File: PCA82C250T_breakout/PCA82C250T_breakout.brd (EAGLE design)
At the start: 100 x 80 mm, 0 parts

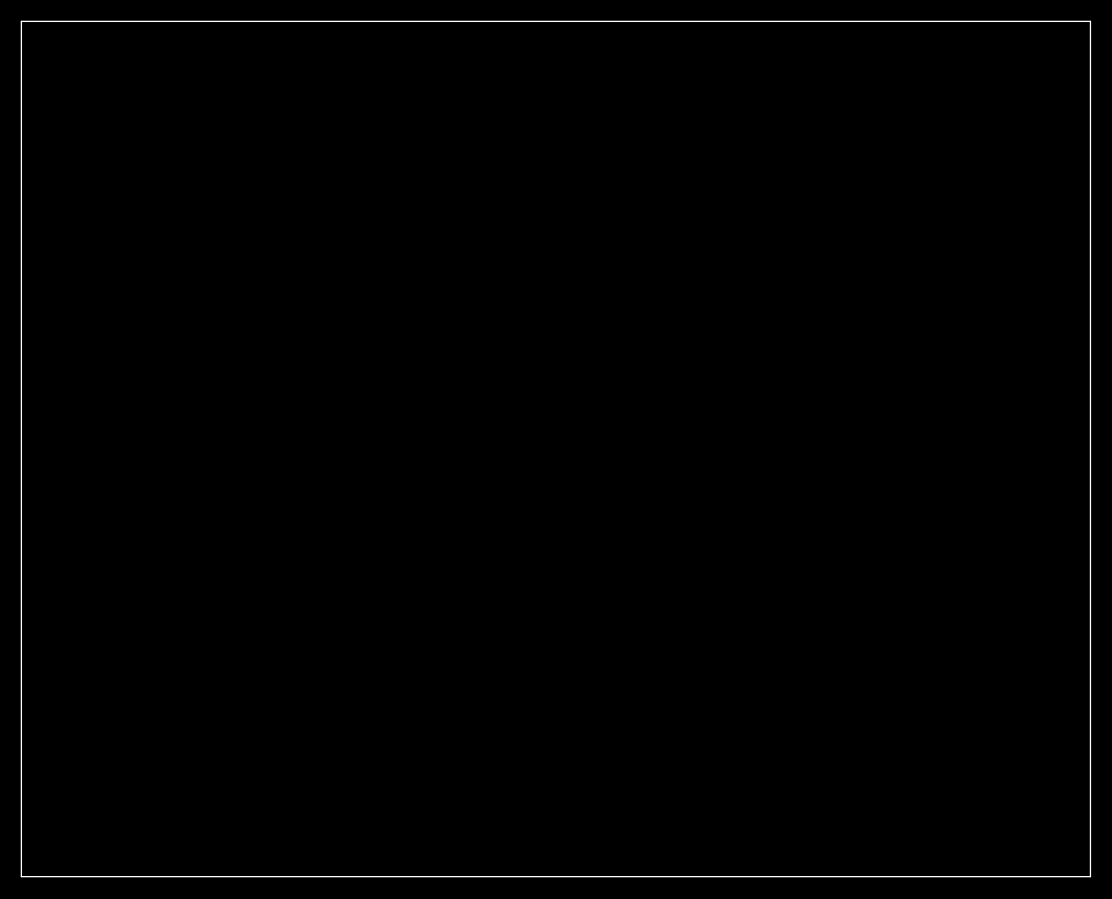
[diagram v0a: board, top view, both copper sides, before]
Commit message: * layed out can breakout PCB
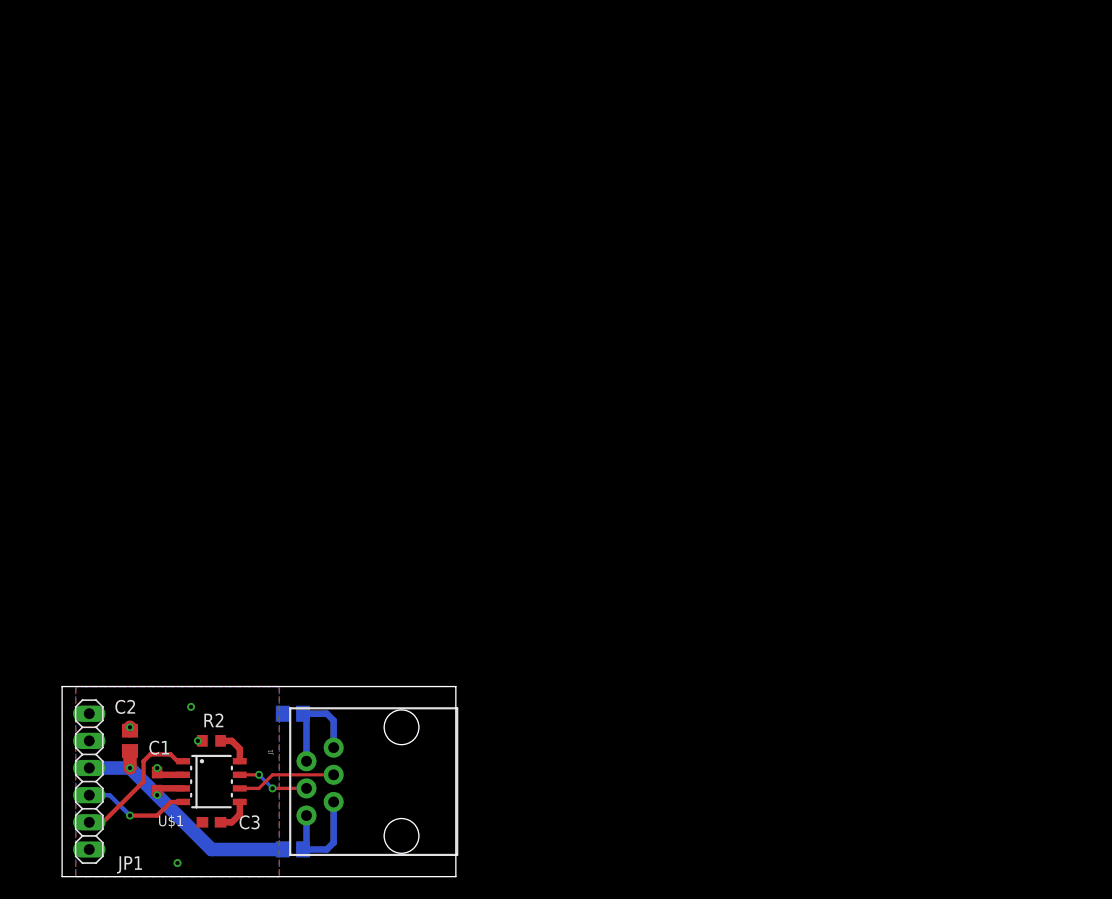
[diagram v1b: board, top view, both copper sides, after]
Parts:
- added C1: 100n, SquantorRCL:C0603
- added C2: 2.2u, SquantorRCL:C0805
- added C3: DNS, SquantorRCL:C0603
- added J1: RJ11, SparkFun-Connectors:RJ11-6
- added JP1: FTDI, SquantorConnectors:1X06
- added R1, R3: FB, SquantorRCL:R0805
- added R2: RS, SquantorRCL:R0603
- added U$1: PCA82C250, SquantorNxp:SOT96-1
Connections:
- new net +5V: C1.2, C2.2, JP1.3, R1.2, U$1.3
- new net CANH: J1.3, U$1.7
- new net CANL: J1.4, U$1.6
- new net GND: C1.1, C2.1, C3.1, JP1.1, R2.2, R3.1, U$1.2
- new net N$1: J1.1, J1.2, R1.1
- new net N$2: C3.2, U$1.5
- new net N$3: J1.5, J1.6, R3.2
- new net N$5: R2.1, U$1.8
- new net UART_RX: JP1.5, U$1.1
- new net UART_TX: JP1.4, U$1.4
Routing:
- net +5V: track 0.00 -> 25.9 mm, vias 0 -> 2
- net UART_RX: track 0.00 -> 12.8 mm
- net N$3: track 0.00 -> 10.1 mm
- net N$1: track 0.00 -> 10.1 mm
- net UART_TX: track 0.00 -> 10.1 mm, vias 0 -> 1
- net CANL: track 0.00 -> 9.31 mm
- net CANH: track 0.00 -> 6.77 mm, vias 0 -> 2
- net GND: track 0.00 -> 3.81 mm, vias 0 -> 5
- net N$2: track 0.00 -> 3.27 mm
- net N$5: track 0.00 -> 3.27 mm
- added copper zone on layer 1, net GND
- added copper zone on layer 16, net GND
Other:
- board size 100 x 80 mm -> 36.8 x 17.8 mm

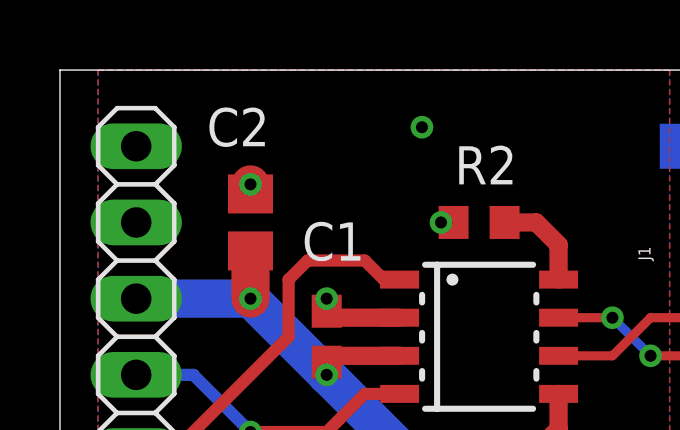
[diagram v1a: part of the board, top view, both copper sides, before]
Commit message: * small mods for OSHpark manufacturing
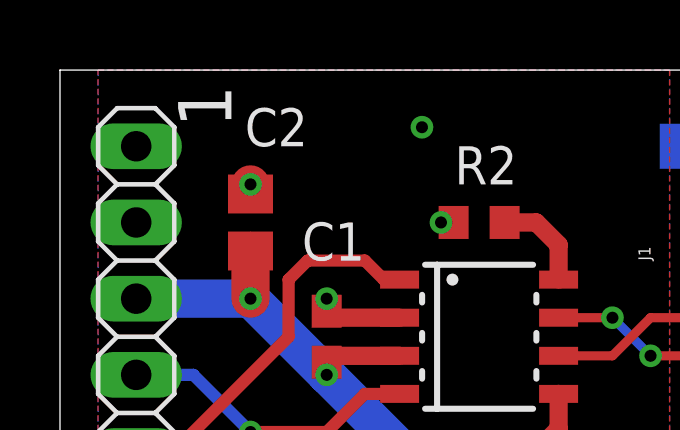
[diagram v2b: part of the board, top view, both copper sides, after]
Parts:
- added LOGO1: OSHW_LOGO_10MILX0200-NT, ohw-logo:OSHW_10X200_NOTEXT
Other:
- board text added: "1"
- board text added: "V2015.10.03"
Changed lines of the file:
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@@
 <wire x1="40.64" y1="17.78" x2="3.81" y2="17.78" width="0" layer="20"/>
 <wire x1="3.81" y1="17.78" x2="3.81" y2="0" width="0" layer="20"/>
+<text x="9.525" y="15.875" size="1.778" layer="25" font="vector" rot="R90">1</text>
+<text x="33.02" y="14.605" size="1.27" layer="26" font="vector" rot="MR270">V2015.10.03</text>
 </plain>
 <attributes>
@@
 <element name="C1" library="SquantorRCL" package="C0603" value="100n" x="12.7" y="8.89" smashed="yes" rot="R270">
 <attribute name="NAME" x="13.97" y="12.7" size="1.27" layer="25" rot="R180"/>
-<attribute name="VALUE" x="15.24" y="14.605" size="1.27" layer="27" rot="R180"/>
+<attribute name="VALUE" x="15.875" y="14.605" size="1.27" layer="27" rot="R180"/>
 </element>
 <element name="C2" library="SquantorRCL" package="C0805" value="2.2u" x="10.16" y="12.7" smashed="yes" rot="R270">
-<attribute name="NAME" x="10.795" y="16.51" size="1.27" layer="25" rot="R180"/>
-<attribute name="VALUE" x="15.24" y="16.51" size="1.27" layer="27" rot="R180"/>
+<attribute name="NAME" x="12.065" y="16.51" size="1.27" layer="25" rot="R180"/>
+<attribute name="VALUE" x="15.875" y="16.51" size="1.27" layer="27" rot="R180"/>
 </element>
 <element name="R1" library="SquantorRCL" package="R0805" value="FB" x="25.4" y="2.54" smashed="yes" rot="MR0">
@@
 <attribute name="VALUE" x="20.955" y="17.145" size="1.27" layer="28" rot="MR180"/>
 </element>
+<element name="LOGO1" library="ohw-logo" package="OSHW_10X200_NOTEXT" value="OSHW_LOGO_10MILX0200-NT" x="20.32" y="6.35" rot="MR0"/>
 </elements>
 <signals>

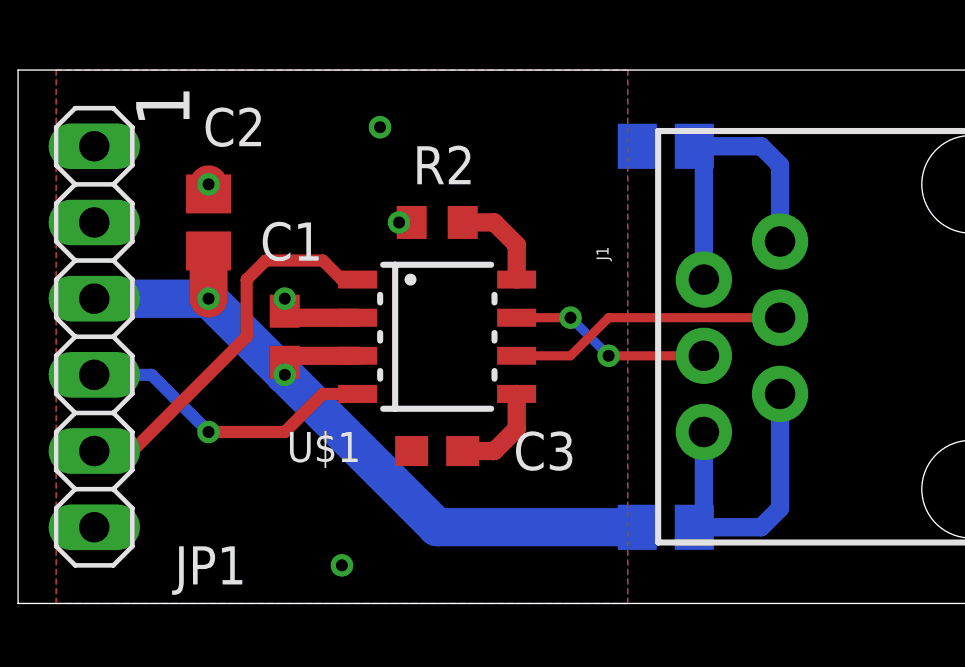
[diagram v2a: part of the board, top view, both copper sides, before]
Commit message: * added CAN termination resistor
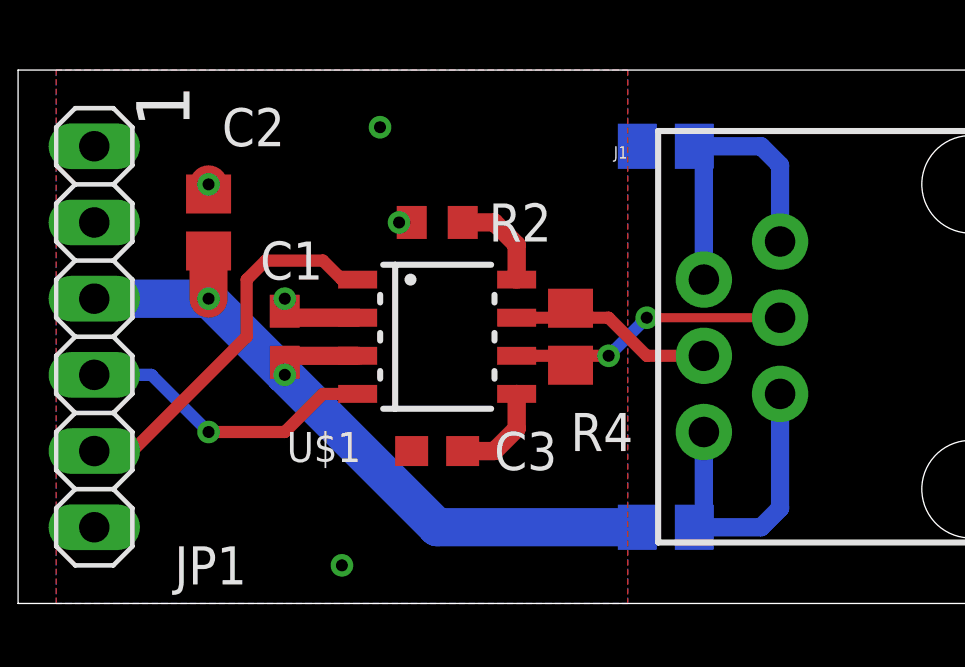
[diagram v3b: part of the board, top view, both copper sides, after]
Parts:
- added R4: 124, SquantorRCL:R0805
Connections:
- net CANH: now also R4.2
- net CANL: now also R4.1
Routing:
- net CANL: track 9.31 -> 9.62 mm, vias 0 -> 2
- net CANH: track 6.77 -> 7.08 mm, vias 2 -> 0
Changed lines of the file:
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@@
 <element name="J1" library="SparkFun-Connectors" package="RJ11-6" value="RJ11" x="35.56" y="8.89" smashed="yes" rot="R90">
 <attribute name="PROD_ID" value="CONN-08590" x="35.56" y="8.89" size="1.778" layer="27" rot="R90" display="off"/>
-<attribute name="NAME" x="23.495" y="11.43" size="0.4064" layer="25" rot="R90"/>
-<attribute name="VALUE" x="22.86" y="11.43" size="0.4064" layer="27" rot="R90"/>
+<attribute name="NAME" x="24.13" y="15.24" size="0.4064" layer="25" rot="R180"/>
+<attribute name="VALUE" x="24.13" y="13.97" size="0.4064" layer="27" rot="R180"/>
 </element>
 <element name="C1" library="SquantorRCL" package="C0603" value="100n" x="12.7" y="8.89" smashed="yes" rot="R270">
-<attribute name="NAME" x="13.97" y="12.7" size="1.27" layer="25" rot="R180"/>
-<attribute name="VALUE" x="15.875" y="14.605" size="1.27" layer="27" rot="R180"/>
+<attribute name="NAME" x="13.97" y="12.065" size="1.27" layer="25" rot="R180"/>
+<attribute name="VALUE" x="15.24" y="13.97" size="1.27" layer="27" rot="R180"/>
 </element>
 <element name="C2" library="SquantorRCL" package="C0805" value="2.2u" x="10.16" y="12.7" smashed="yes" rot="R270">
-<attribute name="NAME" x="12.065" y="16.51" size="1.27" layer="25" rot="R180"/>
-<attribute name="VALUE" x="15.875" y="16.51" size="1.27" layer="27" rot="R180"/>
+<attribute name="NAME" x="12.7" y="16.51" size="1.27" layer="25" rot="R180"/>
+<attribute name="VALUE" x="16.51" y="16.51" size="1.27" layer="27" rot="R180"/>
 </element>
 <element name="R1" library="SquantorRCL" package="R0805" value="FB" x="25.4" y="2.54" smashed="yes" rot="MR0">
@@
 </element>
 <element name="R2" library="SquantorRCL" package="R0603" value="RS" x="17.78" y="12.7" smashed="yes" rot="R180">
-<attribute name="NAME" x="19.05" y="15.24" size="1.27" layer="25" rot="R180"/>
-<attribute name="VALUE" x="19.05" y="17.145" size="1.27" layer="27" rot="R180"/>
+<attribute name="NAME" x="21.59" y="13.335" size="1.27" layer="25" rot="R180"/>
+<attribute name="VALUE" x="21.59" y="15.24" size="1.27" layer="27" rot="R180"/>
 </element>
 <element name="C3" library="SquantorRCL" package="C0603" value="DNS" x="17.78" y="5.08" smashed="yes">
-<attribute name="NAME" x="20.32" y="4.445" size="1.27" layer="25"/>
-<attribute name="VALUE" x="20.32" y="2.54" size="1.27" layer="27"/>
+<attribute name="NAME" x="19.685" y="4.445" size="1.27" layer="25"/>
+<attribute name="VALUE" x="19.685" y="2.54" size="1.27" layer="27"/>
 </element>
 <element name="R3" library="SquantorRCL" package="R0805" value="FB" x="25.4" y="15.24" smashed="yes" rot="MR180">
@@
 </element>
 <element name="LOGO1" library="ohw-logo" package="OSHW_10X200_NOTEXT" value="OSHW_LOGO_10MILX0200-NT" x="20.32" y="6.35" rot="MR0"/>
+<element name="R4" library="SquantorRCL" package="R0805" value="124" x="22.225" y="8.89" smashed="yes" rot="R90">
+<attribute name="NAME" x="22.225" y="5.08" size="1.27" layer="25"/>
+<attribute name="VALUE" x="22.225" y="11.43" size="1.27" layer="27"/>
+</element>
 </elements>
 <signals>
@@
 <contactref element="U$1" pad="7"/>
 <contactref element="J1" pad="3"/>
-<wire x1="26.67" y1="8.255" x2="23.495" y2="8.255" width="0.3048" layer="1"/>
-<via x="23.495" y="8.255" extent="1-16" drill="0.4" shape="octagon"/>
-<wire x1="23.495" y1="8.255" x2="22.225" y2="9.525" width="0.3048" layer="16"/>
-<via x="22.225" y="9.525" extent="1-16" drill="0.4" shape="octagon"/>
-<wire x1="22.225" y1="9.525" x2="20.43" y2="9.525" width="0.3048" layer="1"/>
+<contactref element="R4" pad="2"/>
+<wire x1="20.43" y1="9.525" x2="22.225" y2="9.525" width="0.4064" layer="1"/>
+<wire x1="22.225" y1="9.525" x2="22.225" y2="9.84" width="0.4064" layer="1"/>
+<wire x1="22.225" y1="9.525" x2="23.495" y2="9.525" width="0.4064" layer="1"/>
+<wire x1="23.495" y1="9.525" x2="24.765" y2="8.255" width="0.4064" layer="1"/>
+<wire x1="24.765" y1="8.255" x2="26.67" y2="8.255" width="0.4064" layer="1"/>
 </signal>
 <signal name="CANL">
 <contactref element="U$1" pad="6"/>
 <contactref element="J1" pad="4"/>
-<wire x1="29.21" y1="9.525" x2="23.495" y2="9.525" width="0.3048" layer="1"/>
-<wire x1="23.495" y1="9.525" x2="22.225" y2="8.255" width="0.3048" layer="1"/>
-<wire x1="22.225" y1="8.255" x2="20.43" y2="8.255" width="0.3048" layer="1"/>
+<contactref element="R4" pad="1"/>
+<wire x1="20.43" y1="8.255" x2="22.225" y2="8.255" width="0.4064" layer="1"/>
+<wire x1="22.225" y1="8.255" x2="22.225" y2="7.94" width="0.4064" layer="1"/>
+<wire x1="22.225" y1="8.255" x2="23.495" y2="8.255" width="0.4064" layer="1"/>
+<via x="23.495" y="8.255" extent="1-16" drill="0.4" shape="octagon"/>
+<wire x1="23.495" y1="8.255" x2="24.765" y2="9.525" width="0.4064" layer="16"/>
+<via x="24.765" y="9.525" extent="1-16" drill="0.4" shape="octagon"/>
+<wire x1="29.21" y1="9.525" x2="24.765" y2="9.525" width="0.3048" layer="1"/>
 </signal>
 <signal name="N$2">

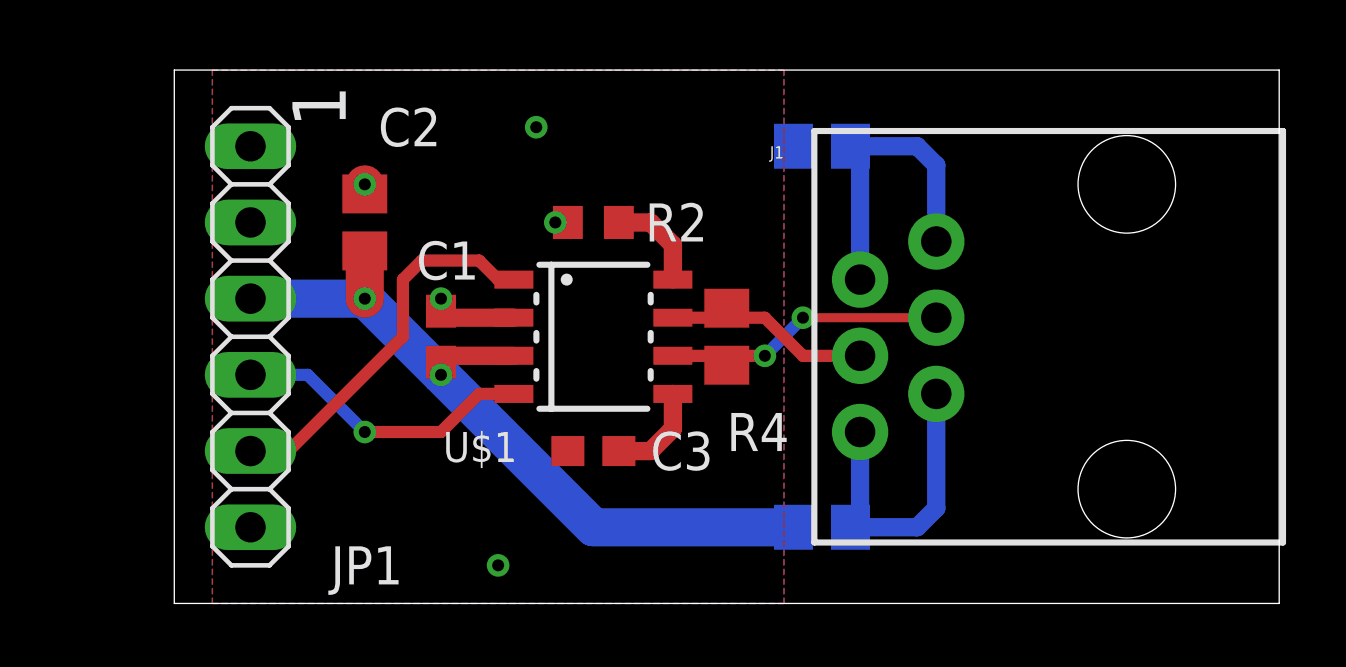
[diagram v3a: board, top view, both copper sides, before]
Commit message: * fixed an RX TX swap, DOH
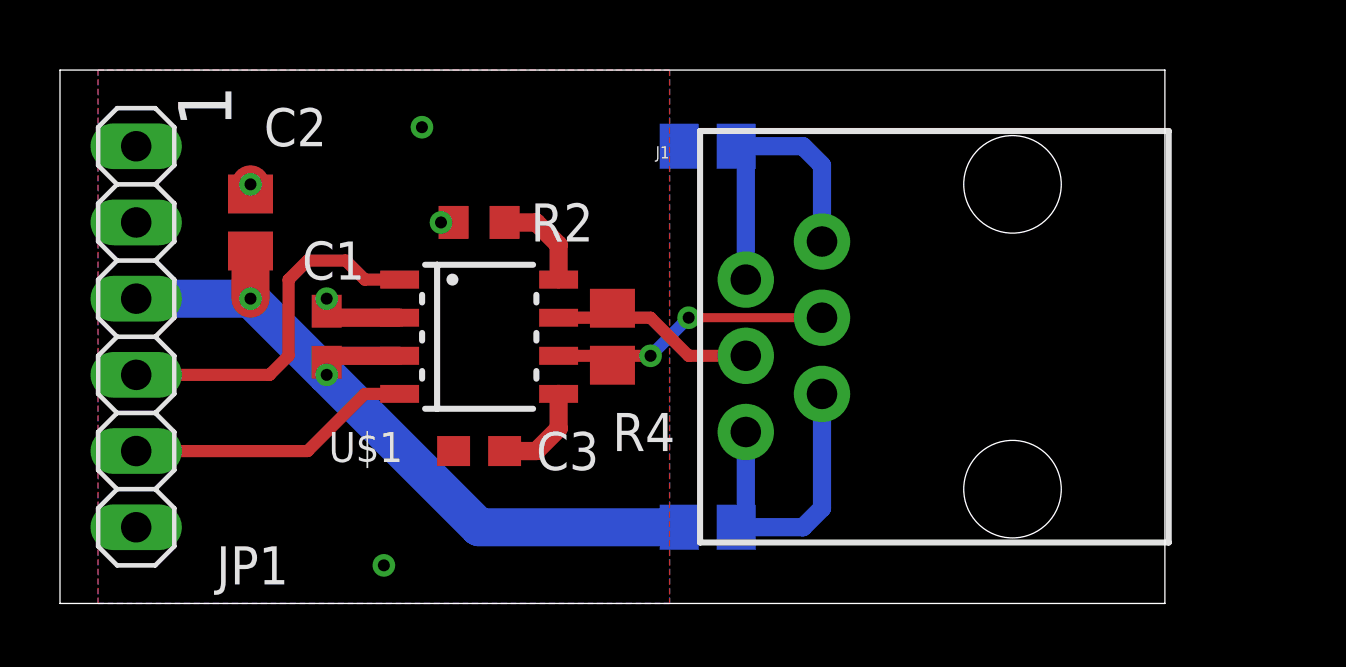
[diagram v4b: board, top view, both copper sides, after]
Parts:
- moved J1 3.81 mm to (31.8, 8.89)
- moved R4 3.81 mm to (18.4, 8.89)
- moved C2 3.81 mm to (6.35, 12.7)
- moved C3 3.81 mm to (14.0, 5.08)
- moved R2 3.81 mm to (14.0, 12.7)
- moved U$1 3.81 mm to (14.0, 8.89)
- moved JP1 3.81 mm to (2.54, 8.89)
- moved C1 3.81 mm to (8.89, 8.89)
- moved LOGO1 3.81 mm to (16.5, 6.35)
- moved R1 3.81 mm to (21.6, 2.54)
- moved R3 3.81 mm to (21.6, 15.2)
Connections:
- net UART_RX: now also U$1.4; no longer U$1.1
- net UART_TX: now also U$1.1; no longer U$1.4
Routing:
- net UART_RX: track 12.8 -> 9.57 mm
- net UART_TX: track 10.1 -> 12.1 mm, vias 1 -> 0
